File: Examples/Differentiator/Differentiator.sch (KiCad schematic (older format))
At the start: 9 parts, among them U1 plot_v1, U2 plot_v1, X1 UA741

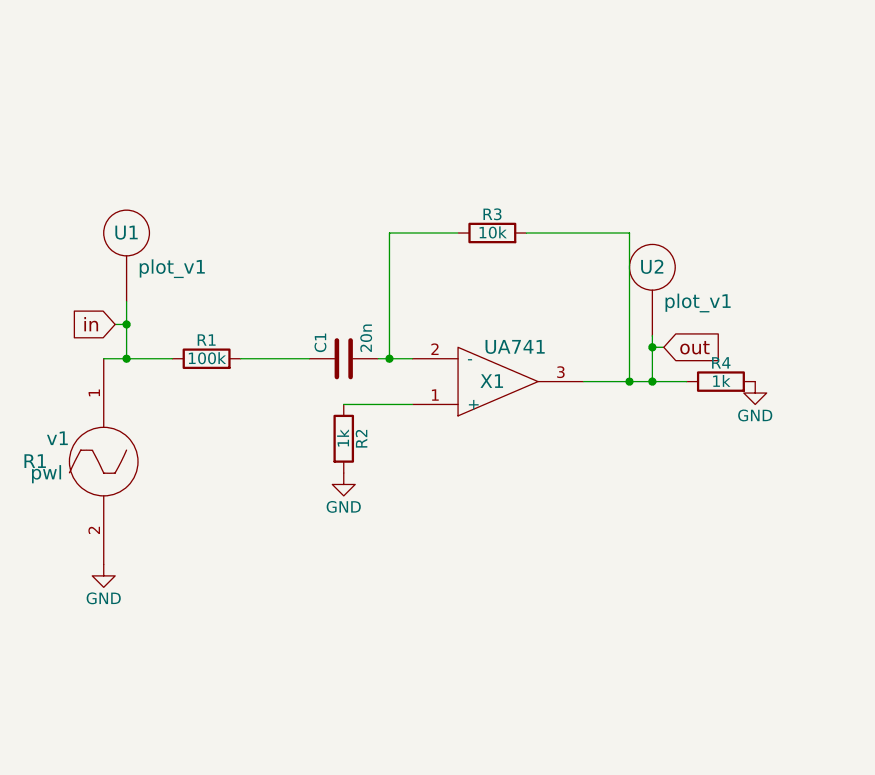
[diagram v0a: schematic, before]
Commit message: common code for Win and Linux, merged py2 changes
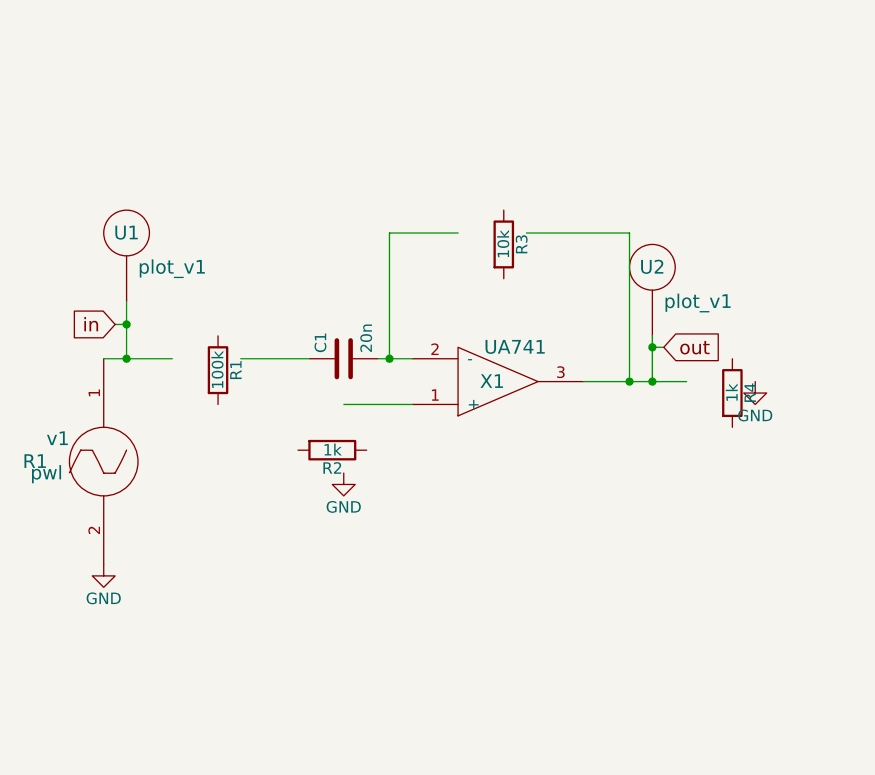
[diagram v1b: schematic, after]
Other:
- moved on the sheet: R1, R2, R3, R4
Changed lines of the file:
@@
 LIBS:74xx
 LIBS:cmos4000
-LIBS:Differentiator-cache
 EELAYER 25 0
 EELAYER END
@@
 L R R3
 U 1 1 56B85BC9
-P 6150 2350
-F 0 "R3" H 6200 2480 50  0000 C CNN
-F 1 "10k" H 6200 2400 50  0000 C CNN
-F 2 "" H 6200 2330 30  0000 C CNN
-F 3 "" V 6200 2400 30  0000 C CNN
-	1    6150 2350
-	1    0    0    -1
+P 6200 2300
+F 0 "R3" H 6250 2430 50  0000 C CNN
+F 1 "10k" H 6250 2350 50  0000 C CNN
+F 2 "" H 6250 2280 30  0000 C CNN
+F 3 "" V 6250 2350 30  0000 C CNN
+	1    6200 2300
+	0    1    1    0
 $EndComp
 $Comp
 L R R1
 U 1 1 56B85C04
-P 4900 2900
-F 0 "R1" H 4950 3030 50  0000 C CNN
-F 1 "100k" H 4950 2950 50  0000 C CNN
-F 2 "" H 4950 2880 30  0000 C CNN
-F 3 "" V 4950 2950 30  0000 C CNN
-	1    4900 2900
-	1    0    0    -1
+P 4950 2850
+F 0 "R1" H 5000 2980 50  0000 C CNN
+F 1 "100k" H 5000 2900 50  0000 C CNN
+F 2 "" H 5000 2830 30  0000 C CNN
+F 3 "" V 5000 2900 30  0000 C CNN
+	1    4950 2850
+	0    1    1    0
 $EndComp
 $Comp
 L R R2
 U 1 1 56B85C6B
-P 5500 3150
-F 0 "R2" H 5550 3280 50  0000 C CNN
-F 1 "1k" H 5550 3200 50  0000 C CNN
-F 2 "" H 5550 3130 30  0000 C CNN
-F 3 "" V 5550 3200 30  0000 C CNN
-	1    5500 3150
-	0    1    1    0
+P 5550 3200
+F 0 "R2" H 5600 3330 50  0000 C CNN
+F 1 "1k" H 5600 3250 50  0000 C CNN
+F 2 "" H 5600 3180 30  0000 C CNN
+F 3 "" V 5600 3250 30  0000 C CNN
+	1    5550 3200
+	-1   0    0    1
 $EndComp
 $Comp
 L R R4
 U 1 1 56B85CD1
-P 7150 3000
-F 0 "R4" H 7200 3130 50  0000 C CNN
-F 1 "1k" H 7200 3050 50  0000 C CNN
-F 2 "" H 7200 2980 30  0000 C CNN
-F 3 "" V 7200 3050 30  0000 C CNN
-	1    7150 3000
-	1    0    0    -1
+P 7200 2950
+F 0 "R4" H 7250 3080 50  0000 C CNN
+F 1 "1k" H 7250 3000 50  0000 C CNN
+F 2 "" H 7250 2930 30  0000 C CNN
+F 3 "" V 7250 3000 30  0000 C CNN
+	1    7200 2950
+	0    1    1    0
 $EndComp
 $Comp

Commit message: fixing library preferences
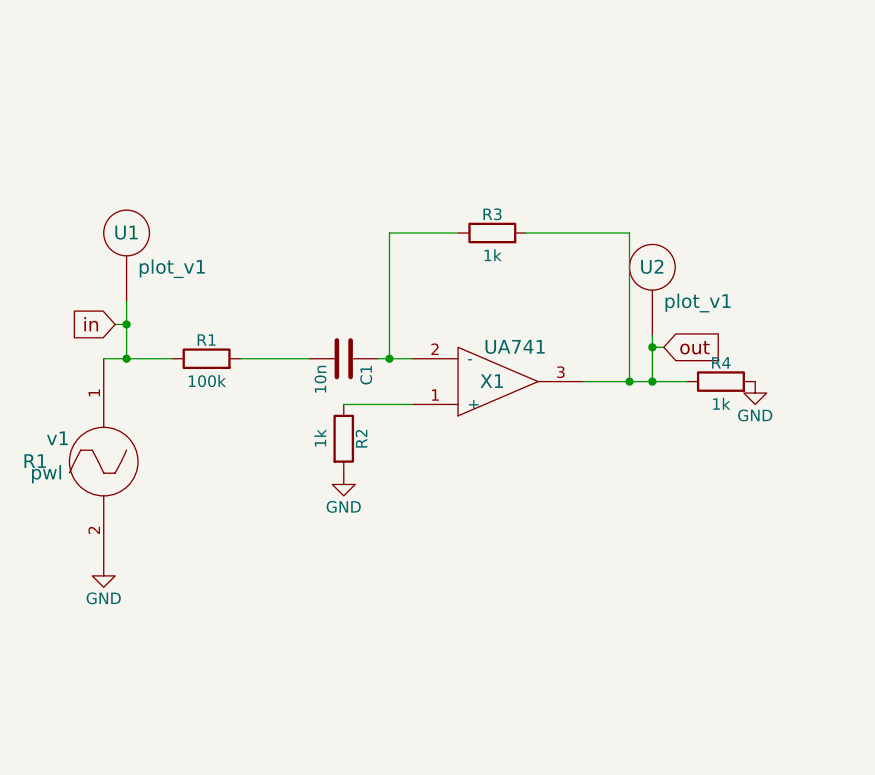
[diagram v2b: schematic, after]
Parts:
- removed C1: 20n, symbol C
- removed R1: 100k, symbol R
- removed R2, R4: 1k, symbol R
- removed R3: 10k, symbol R
- added C1: 10n, symbol capacitor
- added R1: 100k, symbol resistor
- added R2, R3, R4: 1k, symbol resistor
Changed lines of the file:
@@
 LIBS:contrib
 LIBS:power
-LIBS:device
 LIBS:transistors
 LIBS:conn
-LIBS:linear
 LIBS:regul
 LIBS:74xx
 LIBS:cmos4000
+LIBS:Differentiator-cache
 EELAYER 25 0
 EELAYER END
@@
 $EndComp
 $Comp
-L R R3
-U 1 1 56B85BC9
-P 6200 2300
-F 0 "R3" H 6250 2430 50  0000 C CNN
-F 1 "10k" H 6250 2350 50  0000 C CNN
-F 2 "" H 6250 2280 30  0000 C CNN
-F 3 "" V 6250 2350 30  0000 C CNN
-	1    6200 2300
-	0    1    1    0
-$EndComp
-$Comp
-L R R1
-U 1 1 56B85C04
-P 4950 2850
-F 0 "R1" H 5000 2980 50  0000 C CNN
-F 1 "100k" H 5000 2900 50  0000 C CNN
-F 2 "" H 5000 2830 30  0000 C CNN
-F 3 "" V 5000 2900 30  0000 C CNN
-	1    4950 2850
-	0    1    1    0
-$EndComp
-$Comp
-L R R2
-U 1 1 56B85C6B
-P 5550 3200
-F 0 "R2" H 5600 3330 50  0000 C CNN
-F 1 "1k" H 5600 3250 50  0000 C CNN
-F 2 "" H 5600 3180 30  0000 C CNN
-F 3 "" V 5600 3250 30  0000 C CNN
-	1    5550 3200
-	-1   0    0    1
-$EndComp
-$Comp
-L R R4
-U 1 1 56B85CD1
-P 7200 2950
-F 0 "R4" H 7250 3080 50  0000 C CNN
-F 1 "1k" H 7250 3000 50  0000 C CNN
-F 2 "" H 7250 2930 30  0000 C CNN
-F 3 "" V 7250 3000 30  0000 C CNN
-	1    7200 2950
-	0    1    1    0
-$EndComp
-$Comp
-L C C1
-U 1 1 56B85D7C
-P 5550 2850
-F 0 "C1" H 5575 2950 50  0000 L CNN
-F 1 "20n" H 5575 2750 50  0000 L CNN
-F 2 "" H 5588 2700 30  0000 C CNN
-F 3 "" H 5550 2850 60  0000 C CNN
-	1    5550 2850
-	0    -1   -1   0
-$EndComp
-$Comp
 L pwl v1
 U 1 1 56B85E24
@@
 $EndComp
 $Comp
-L GND #PWR01
+L GND #PWR1
 U 1 1 56B85ECF
 P 4500 3750
-F 0 "#PWR01" H 4500 3500 50  0001 C CNN
+F 0 "#PWR1" H 4500 3500 50  0001 C CNN
 F 1 "GND" H 4500 3600 50  0000 C CNN
 F 2 "" H 4500 3750 50  0000 C CNN
@@
 $EndComp
 $Comp
-L GND #PWR02
+L GND #PWR2
 U 1 1 56B85EF6
 P 5550 3350
-F 0 "#PWR02" H 5550 3100 50  0001 C CNN
+F 0 "#PWR2" H 5550 3100 50  0001 C CNN
 F 1 "GND" H 5550 3200 50  0000 C CNN
 F 2 "" H 5550 3350 50  0000 C CNN
@@
 $EndComp
 $Comp
-L GND #PWR03
+L GND #PWR3
 U 1 1 56B85F16
 P 7350 2950
-F 0 "#PWR03" H 7350 2700 50  0001 C CNN
+F 0 "#PWR3" H 7350 2700 50  0001 C CNN
 F 1 "GND" H 7350 2800 50  0000 C CNN
 F 2 "" H 7350 2950 50  0000 C CNN
@@
 Connection ~ 4600 2700
 Connection ~ 6900 2800
+$Comp
+L resistor R1
+U 1 1 5E68BD57
+P 4900 2900
+F 0 "R1" H 4950 3030 50  0000 C CNN
+F 1 "100k" H 4950 2850 50  0000 C CNN
+F 2 "" H 4950 2880 30  0000 C CNN
+F 3 "" V 4950 2950 30  0000 C CNN
+	1    4900 2900
+	1    0    0    -1
+$EndComp
+$Comp
+L capacitor C1
+U 1 1 5E68BE9A
+P 5550 2850
+F 0 "C1" H 5575 2950 50  0000 L CNN
+F 1 "10n" H 5575 2750 50  0000 L CNN
+F 2 "" H 5588 2700 30  0000 C CNN
+F 3 "" H 5550 2850 60  0000 C CNN
+	1    5550 2850
+	0    1    1    0
+$EndComp
+$Comp
+L resistor R2
+U 1 1 5E68BF22
+P 5500 3150
+F 0 "R2" H 5550 3280 50  0000 C CNN
+F 1 "1k" H 5550 3100 50  0000 C CNN
+F 2 "" H 5550 3130 30  0000 C CNN
+F 3 "" V 5550 3200 30  0000 C CNN
+	1    5500 3150
+	0    1    1    0
+$EndComp
+$Comp
+L resistor R3
+U 1 1 5E68BFEA
+P 6150 2350
+F 0 "R3" H 6200 2480 50  0000 C CNN
+F 1 "1k" H 6200 2300 50  0000 C CNN
+F 2 "" H 6200 2330 30  0000 C CNN
+F 3 "" V 6200 2400 30  0000 C CNN
+	1    6150 2350
+	1    0    0    -1
+$EndComp
+$Comp
+L resistor R4
+U 1 1 5E68C095
+P 7150 3000
+F 0 "R4" H 7200 3130 50  0000 C CNN
+F 1 "1k" H 7200 2950 50  0000 C CNN
+F 2 "" H 7200 2980 30  0000 C CNN
+F 3 "" V 7200 3050 30  0000 C CNN
+	1    7150 3000
+	1    0    0    -1
+$EndComp
 $EndSCHEMATC

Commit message: Precision Rectifier example added
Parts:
- removed X1: UA741, symbol UA741
- added X1: lm_741, symbol lm_741
- added v2, v3: DC, R1, symbol DC
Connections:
- wire segments 13 -> 20
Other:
- moved on the sheet: R2, R3, R4, U2
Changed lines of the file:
@@
 $EndDescr
-$Comp
-L UA741 X1
-U 1 1 56B85B7E
-P 6050 2950
-F 0 "X1" H 6200 2950 60  0000 C CNN
-F 1 "UA741" H 6300 2800 60  0000 C CNN
-F 2 "" H 6050 2950 60  0000 C CNN
-F 3 "" H 6050 2950 60  0000 C CNN
-	1    6050 2950
-	1    0    0    1
-$EndComp
 $Comp
 L pwl v1
@@
 $EndComp
 $Comp
-L GND #PWR1
+L GND #PWR01
 U 1 1 56B85ECF
-P 4500 3750
-F 0 "#PWR1" H 4500 3500 50  0001 C CNN
-F 1 "GND" H 4500 3600 50  0000 C CNN
-F 2 "" H 4500 3750 50  0000 C CNN
-F 3 "" H 4500 3750 50  0000 C CNN
-	1    4500 3750
-	1    0    0    -1
-$EndComp
-$Comp
-L GND #PWR2
+P 4500 3900
+F 0 "#PWR01" H 4500 3650 50  0001 C CNN
+F 1 "GND" H 4500 3750 50  0000 C CNN
+F 2 "" H 4500 3900 50  0000 C CNN
+F 3 "" H 4500 3900 50  0000 C CNN
+	1    4500 3900
+	1    0    0    -1
+$EndComp
+$Comp
+L GND #PWR02
 U 1 1 56B85EF6
-P 5550 3350
-F 0 "#PWR2" H 5550 3100 50  0001 C CNN
-F 1 "GND" H 5550 3200 50  0000 C CNN
-F 2 "" H 5550 3350 50  0000 C CNN
-F 3 "" H 5550 3350 50  0000 C CNN
-	1    5550 3350
-	1    0    0    -1
-$EndComp
-$Comp
-L GND #PWR3
+P 5550 3400
+F 0 "#PWR02" H 5550 3150 50  0001 C CNN
+F 1 "GND" H 5550 3250 50  0000 C CNN
+F 2 "" H 5550 3400 50  0000 C CNN
+F 3 "" H 5550 3400 50  0000 C CNN
+	1    5550 3400
+	1    0    0    -1
+$EndComp
+$Comp
+L GND #PWR03
 U 1 1 56B85F16
-P 7350 2950
-F 0 "#PWR3" H 7350 2700 50  0001 C CNN
-F 1 "GND" H 7350 2800 50  0000 C CNN
-F 2 "" H 7350 2950 50  0000 C CNN
-F 3 "" H 7350 2950 50  0000 C CNN
-	1    7350 2950
+P 7700 3000
+F 0 "#PWR03" H 7700 2750 50  0001 C CNN
+F 1 "GND" H 7700 2850 50  0000 C CNN
+F 2 "" H 7700 3000 50  0000 C CNN
+F 3 "" H 7700 3000 50  0000 C CNN
+	1    7700 3000
 	1    0    0    -1
 $EndComp
@@
 	5700 2850 5850 2850
 Wire Wire Line
-	5850 3050 5550 3050
-Wire Wire Line
-	6600 2950 7050 2950
-Wire Wire Line
-	6350 2300 6800 2300
-Wire Wire Line
-	6800 2300 6800 2950
-Connection ~ 6800 2950
-Wire Wire Line
-	6050 2300 5750 2300
-Wire Wire Line
-	5750 2300 5750 2850
+	5850 3100 5550 3100
+Wire Wire Line
+	6950 3000 7400 3000
+Wire Wire Line
+	6700 2350 7150 2350
+Wire Wire Line
+	7150 2350 7150 3000
+Connection ~ 7150 3000
 Connection ~ 5750 2850
 Text GLabel 4550 2700 0    60   Input ~ 0
 in
-Text GLabel 6950 2800 2    60   Input ~ 0
+Text GLabel 7300 2850 2    60   Input ~ 0
 out
 Wire Wire Line
@@
 Connection ~ 4600 2850
 Wire Wire Line
-	6950 2800 6900 2800
-Wire Wire Line
-	6900 2750 6900 2950
-Connection ~ 6900 2950
+	7300 2850 7250 2850
+Wire Wire Line
+	7250 2800 7250 3000
+Connection ~ 7250 3000
 $Comp
 L plot_v1 U1
@@
 L plot_v1 U2
 U 1 1 56D46C5F
-P 6900 2950
-F 0 "U2" H 6900 3450 60  0000 C CNN
-F 1 "plot_v1" H 7100 3300 60  0000 C CNN
-F 2 "" H 6900 2950 60  0000 C CNN
-F 3 "" H 6900 2950 60  0000 C CNN
-	1    6900 2950
+P 7250 3000
+F 0 "U2" H 7250 3500 60  0000 C CNN
+F 1 "plot_v1" H 7450 3350 60  0000 C CNN
+F 2 "" H 7250 3000 60  0000 C CNN
+F 3 "" H 7250 3000 60  0000 C CNN
+	1    7250 3000
 	1    0    0    -1
 $EndComp
 Connection ~ 4600 2700
-Connection ~ 6900 2800
+Connection ~ 7250 2850
 $Comp
 L resistor R1
@@
 L resistor R2
 U 1 1 5E68BF22
-P 5500 3150
-F 0 "R2" H 5550 3280 50  0000 C CNN
-F 1 "1k" H 5550 3100 50  0000 C CNN
-F 2 "" H 5550 3130 30  0000 C CNN
-F 3 "" V 5550 3200 30  0000 C CNN
-	1    5500 3150
+P 5500 3200
+F 0 "R2" H 5550 3330 50  0000 C CNN
+F 1 "1k" H 5550 3150 50  0000 C CNN
+F 2 "" H 5550 3180 30  0000 C CNN
+F 3 "" V 5550 3250 30  0000 C CNN
+	1    5500 3200
 	0    1    1    0
 $EndComp
@@
 L resistor R3
 U 1 1 5E68BFEA
-P 6150 2350
-F 0 "R3" H 6200 2480 50  0000 C CNN
-F 1 "1k" H 6200 2300 50  0000 C CNN
-F 2 "" H 6200 2330 30  0000 C CNN
-F 3 "" V 6200 2400 30  0000 C CNN
-	1    6150 2350
+P 6500 2400
+F 0 "R3" H 6550 2530 50  0000 C CNN
+F 1 "1k" H 6550 2350 50  0000 C CNN
+F 2 "" H 6550 2380 30  0000 C CNN
+F 3 "" V 6550 2450 30  0000 C CNN
+	1    6500 2400
 	1    0    0    -1
 $EndComp
@@
 L resistor R4
 U 1 1 5E68C095
-P 7150 3000
-F 0 "R4" H 7200 3130 50  0000 C CNN
-F 1 "1k" H 7200 2950 50  0000 C CNN
-F 2 "" H 7200 2980 30  0000 C CNN
-F 3 "" V 7200 3050 30  0000 C CNN
-	1    7150 3000
-	1    0    0    -1
-$EndComp
+P 7500 3050
+F 0 "R4" H 7550 3180 50  0000 C CNN
+F 1 "1k" H 7550 3000 50  0000 C CNN
+F 2 "" H 7550 3030 30  0000 C CNN
+F 3 "" V 7550 3100 30  0000 C CNN
+	1    7500 3050
+	1    0    0    -1
+$EndComp
+$Comp
+L lm_741 X1
+U 1 1 5E7DF220
+P 6400 3000
+F 0 "X1" H 6200 3000 60  0000 C CNN
+F 1 "lm_741" H 6300 2750 60  0000 C CNN
+F 2 "" H 6400 3000 60  0000 C CNN
+F 3 "" H 6400 3000 60  0000 C CNN
+	1    6400 3000
+	1    0    0    -1
+$EndComp
+$Comp
+L DC v3
+U 1 1 5E7DF2B6
+P 5750 1950
+F 0 "v3" H 5550 2050 60  0000 C CNN
+F 1 "DC" H 5550 1900 60  0000 C CNN
+F 2 "R1" H 5450 1950 60  0000 C CNN
+F 3 "" H 5750 1950 60  0000 C CNN
+	1    5750 1950
+	0    1    1    0
+$EndComp
+Wire Wire Line
+	6200 1950 6250 1950
+Wire Wire Line
+	6250 1950 6250 2550
+$Comp
+L GND #PWR04
+U 1 1 5E7DF3B7
+P 5100 1950
+F 0 "#PWR04" H 5100 1700 50  0001 C CNN
+F 1 "GND" H 5100 1800 50  0000 C CNN
+F 2 "" H 5100 1950 50  0000 C CNN
+F 3 "" H 5100 1950 50  0000 C CNN
+	1    5100 1950
+	0    1    1    0
+$EndComp
+Wire Wire Line
+	5100 1950 5300 1950
+$Comp
+L DC v2
+U 1 1 5E7DF447
+P 5700 4000
+F 0 "v2" H 5500 4100 60  0000 C CNN
+F 1 "DC" H 5500 3950 60  0000 C CNN
+F 2 "R1" H 5400 4000 60  0000 C CNN
+F 3 "" H 5700 4000 60  0000 C CNN
+	1    5700 4000
+	0    -1   -1   0
+$EndComp
+Wire Wire Line
+	6150 4000 6250 4000
+$Comp
+L GND #PWR05
+U 1 1 5E7DF44E
+P 5050 4000
+F 0 "#PWR05" H 5050 3750 50  0001 C CNN
+F 1 "GND" H 5050 3850 50  0000 C CNN
+F 2 "" H 5050 4000 50  0000 C CNN
+F 3 "" H 5050 4000 50  0000 C CNN
+	1    5050 4000
+	0    1    1    0
+$EndComp
+Wire Wire Line
+	5050 4000 5250 4000
+Wire Wire Line
+	6250 4000 6250 3450
+Wire Wire Line
+	6400 2350 5750 2350
+Wire Wire Line
+	5750 2350 5750 2850
+Wire Wire Line
+	4500 3900 4500 3750
 $EndSCHEMATC
